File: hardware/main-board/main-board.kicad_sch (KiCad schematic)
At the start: 58 parts, among them J14 Top Left(M), J16 Top Right (M), J18 Bottom Left(M), J20 Bottom Right(M), J9 PWR, Q1 MMBFJ201, U1 TL074, U2 AS3340, U3 79L05, U4 LP2950

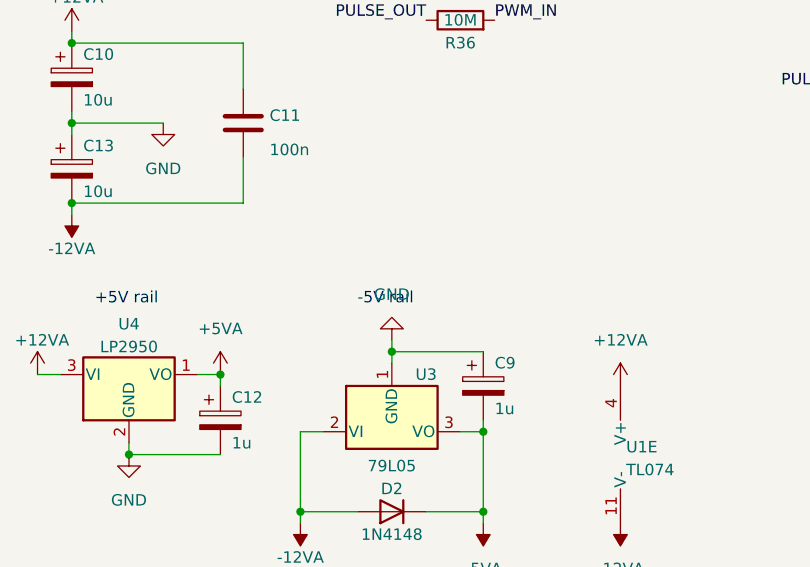
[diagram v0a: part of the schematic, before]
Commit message: chore: git improvements
Using git submodules for managing shared libraries.
Extracted a shared release workflow build to centralise this common
aspect.
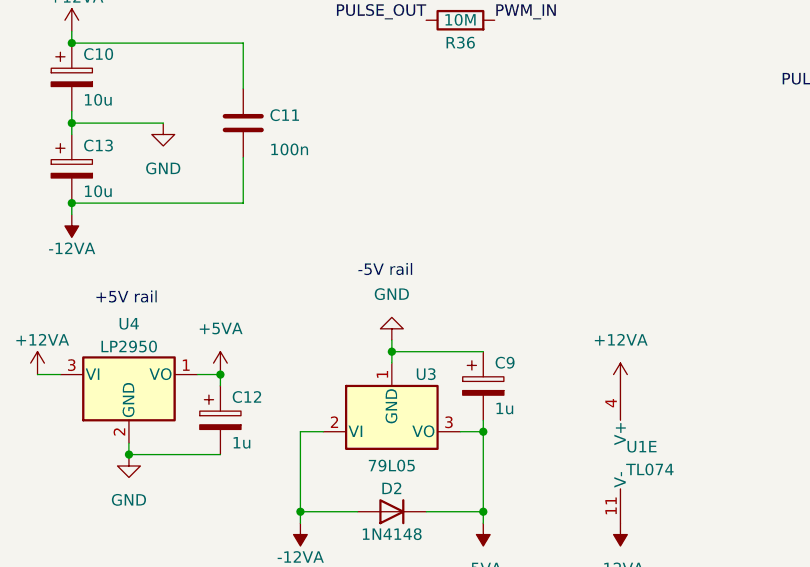
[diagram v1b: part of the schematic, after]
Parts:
- J9: footprint Eurorack Common:SHDR10W50P254_2X5_2020X850X920P -> Eurorack Common:Eurorack Power Header (10 pin); symbol Connector_Generic:Conn_02x05_Odd_Even -> Eurorack Common:Eurorack_Power_Header_(10_pin)
- Q1: symbol cem-3340:MMBFJ201 -> Eurorack Common:MMBFJ201
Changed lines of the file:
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@@
 	(text "-5V rail"
 		(exclude_from_sim no)
-		(at 130.81 163.83 0)
+		(at 130.81 160.782 0)
 		(effects
 			(font
@@
 	)
 	(symbol
-		(lib_id "Connector_Generic:Conn_02x05_Odd_Even")
+		(lib_id "Eurorack Common:Eurorack_Power_Header_(10_pin)")
 		(at 115.57 104.14 0)
 		(unit 1)
@@
 			)
 		)
-		(property "Footprint" "Eurorack Common:SHDR10W50P254_2X5_2020X850X920P"
+		(property "Footprint" "Eurorack Common:Eurorack Power Header (10 pin)"
 			(at 115.57 104.14 0)
 			(effects
@@
 	)
 	(symbol
-		(lib_id "cem-3340:MMBFJ201")
+		(lib_id "Eurorack Common:MMBFJ201")
 		(at 212.09 40.64 0)
 		(unit 1)

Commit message: feature: docs
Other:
- title: (none) -> CEM3340 VCO - Main Board
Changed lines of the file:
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@@
 	(generator_version "9.0")
 	(paper "A4")
+	(title_block
+		(title "CEM3340 VCO - Main Board")
+		(date "2025-11-05")
+		(rev "v1.0.0")
+	)
 	(text "Power decoupling"
 		(exclude_from_sim no)

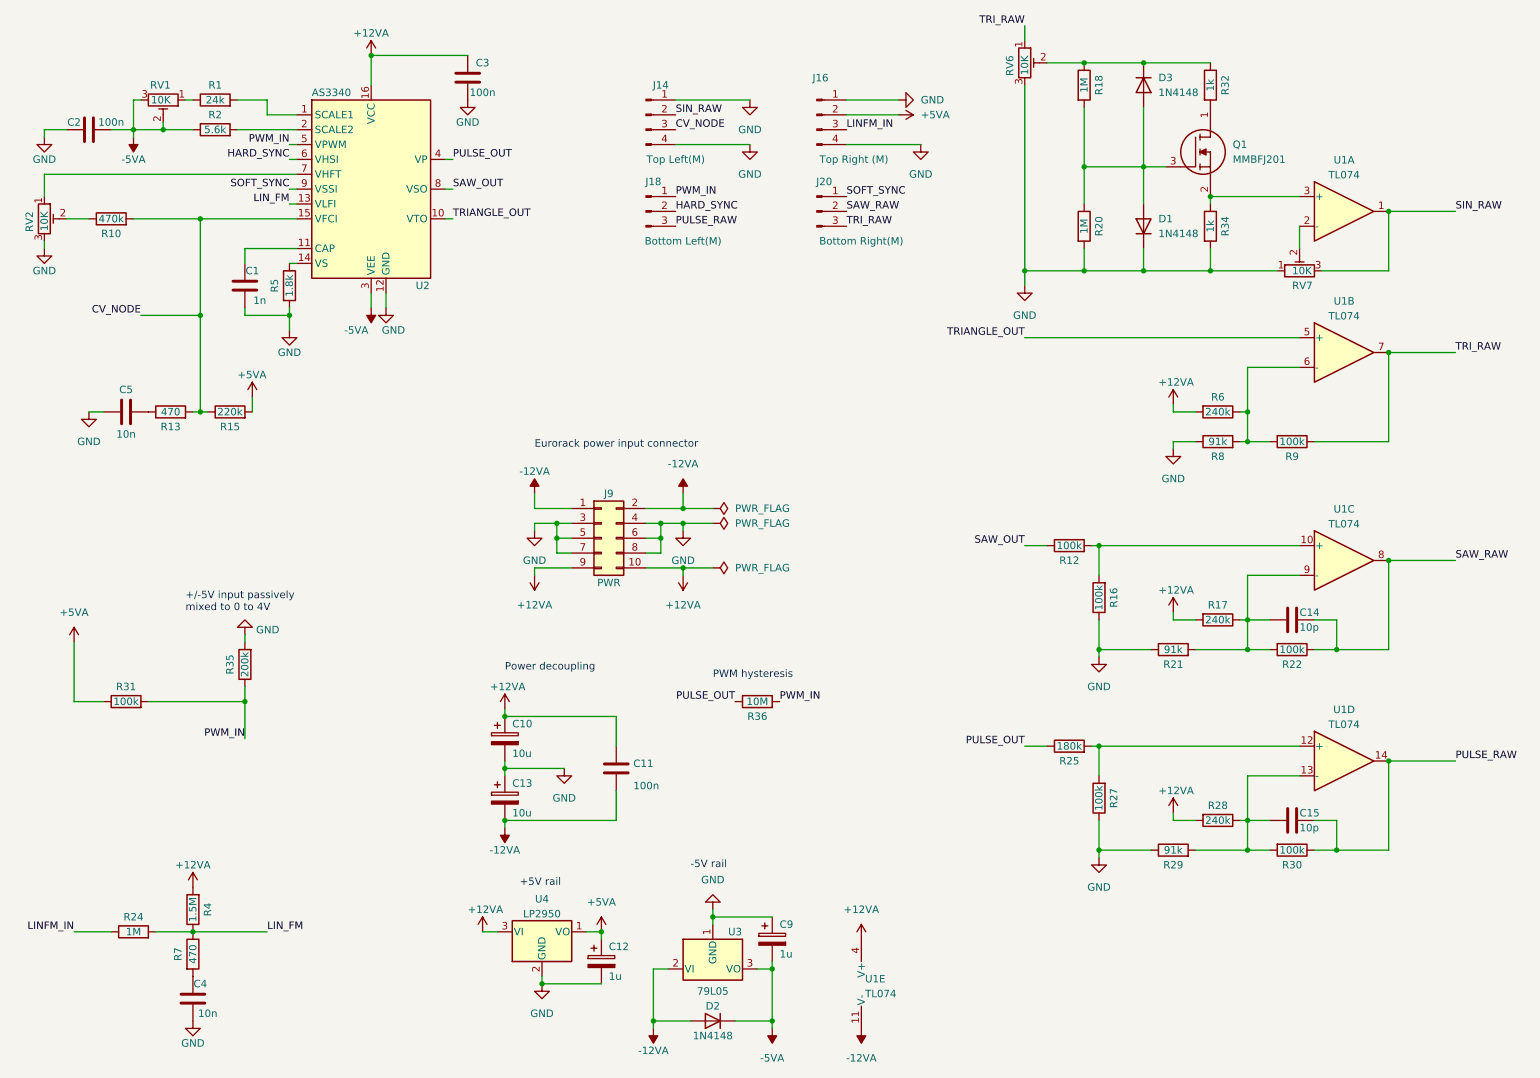
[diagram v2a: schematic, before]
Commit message: feature: improve docs + front panel design
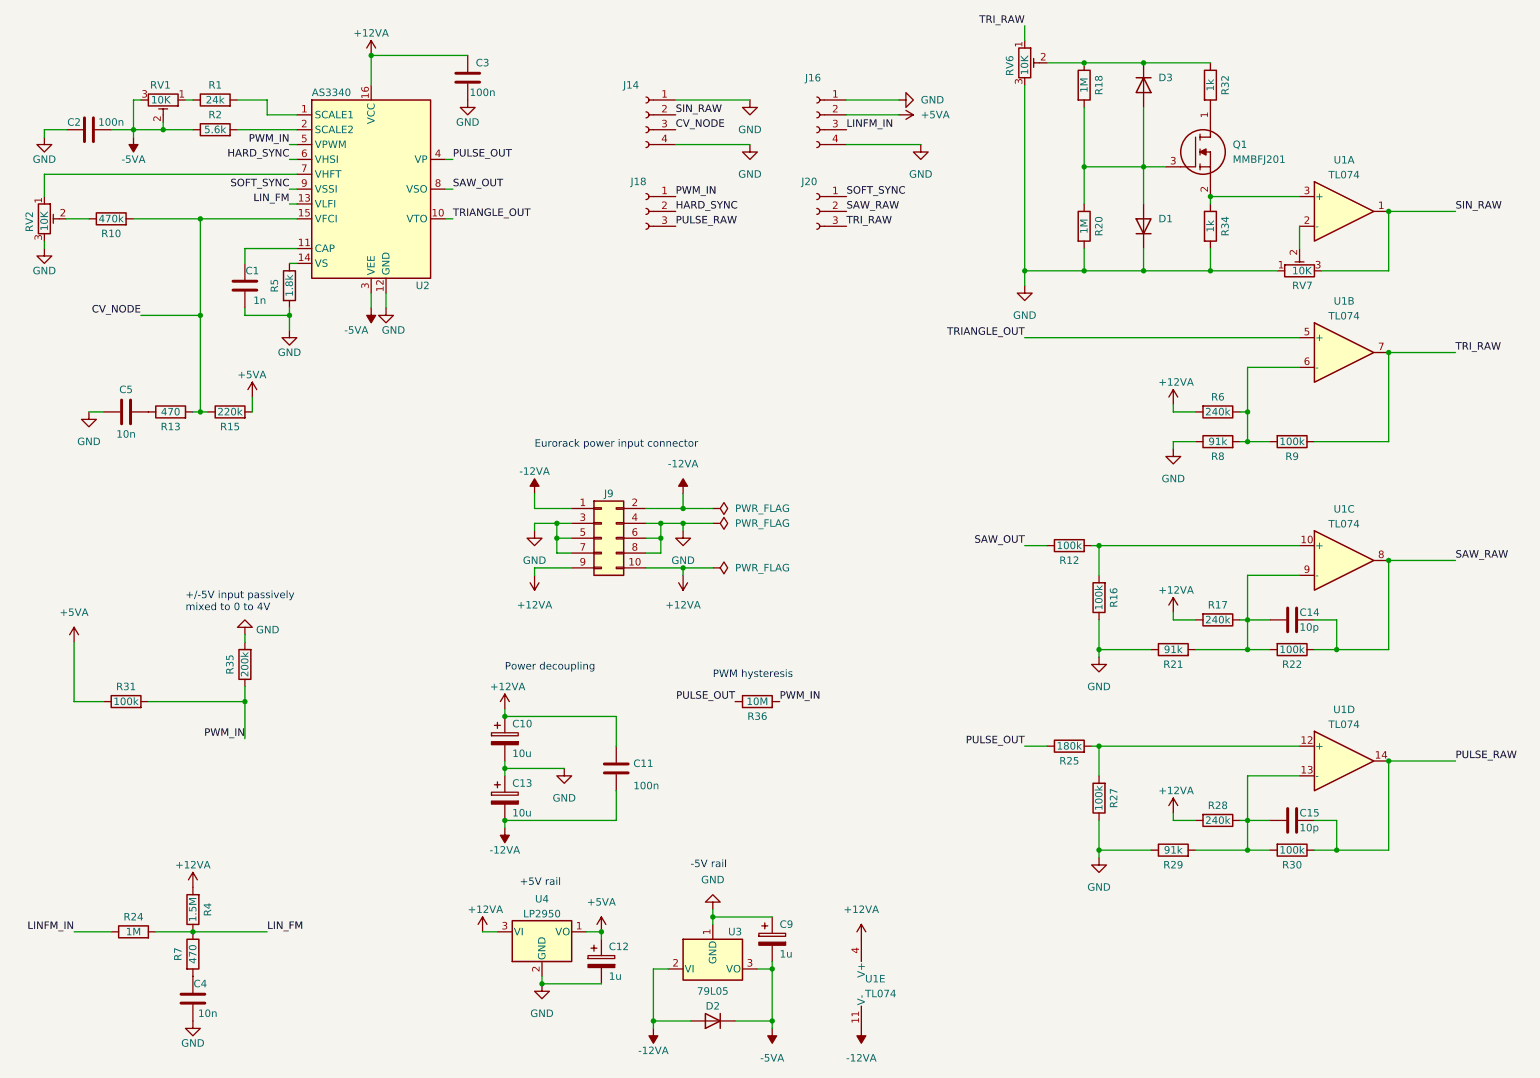
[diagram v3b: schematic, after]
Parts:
- C1: footprint Capacitor_THT:C_Rect_L4.6mm_W2.0mm_P2.50mm_MKS02_FKP02 -> Eurorack Common:C_Disc_D3.4mm_W2.1mm_P2.50mm; Note (none) -> C0G/NP0 ceramic, 2.5mm pitch; Reference_Part (none) -> C320C102J1G5TA; Tolerance (none) -> 5%
- C10, C13: footprint Capacitor_THT:CP_Radial_D5.0mm_P2.00mm -> Eurorack Common:CP_Radial_D5.0mm_H11.0mm_P2.00mm; Note (none) -> Electrolytic, min. 25V, *max height 11mm*, diameter 5mm, pi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; Reference_Part (none) -> ESH106M050AC3AA; Tolerance (none) -> 20%
- C11, C2, C3: footprint Capacitor_THT:C_Rect_L4.6mm_W3.0mm_P2.50mm_MKS02_FKP02 -> Eurorack Common:C_Disc_D3.4mm_W2.1mm_P2.50mm; Note (none) -> X7R ceramic, 2.5mm pitch; Reference_Part (none) -> C320C104K5R5TA; Tolerance (none) -> 5%
- C12, C9: footprint Capacitor_THT:CP_Radial_D4.0mm_P1.50mm -> Eurorack Common:CP_Radial_D4.0mm_P1.50mm; Note (none) -> Electrolytic, min. 25V, *max height 11mm*, diameter 4mm, pi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; Reference_Part (none) -> UST1H010MDD; Tolerance (none) -> 20%
- C14, C15: footprint Capacitor_THT:C_Rect_L4.0mm_W2.5mm_P2.50mm -> Eurorack Common:C_Disc_D3.4mm_W2.1mm_P2.50mm; Note (none) -> C0G/NP0 ceramic, 2.5mm pitch; Reference_Part (none) -> K100J15C0GF5TL2; Tolerance (none) -> 5%
- C4, C5: footprint Capacitor_THT:C_Rect_L4.6mm_W3.0mm_P2.50mm_MKS02_FKP02 -> Eurorack Common:C_Disc_D3.4mm_W2.1mm_P2.50mm; Note (none) -> X7R ceramic, 2.5mm pitch; Reference_Part (none) -> C322C103K1R5TA; Tolerance (none) -> 5%
- D1, D2, D3: value 1N4148 -> ~; footprint Diode_THT:D_DO-35_SOD27_P7.62mm_Horizontal -> Eurorack Common:D_DO-35_SOD27_P7.62mm_Horizontal; Reference_Part (none) -> 1N4148
- J14: value Top Left(M) -> ~; footprint Connector_PinHeader_2.54mm:PinHeader_1x04_P2.54mm_Vertical -> Eurorack Common:PinSocket_1x04_P2.54mm_Vertical; symbol Connector:Conn_01x04_Pin -> Connector:Conn_01x04_Socket; Reference_Part (none) -> 1x4 socket header
- J16: value Top Right (M) -> ~; footprint Connector_PinHeader_2.54mm:PinHeader_1x04_P2.54mm_Vertical -> Eurorack Common:PinSocket_1x04_P2.54mm_Vertical; symbol Connector:Conn_01x04_Pin -> Connector:Conn_01x04_Socket; Reference_Part (none) -> 1x4 socket header
- J18: value Bottom Left(M) -> ~; footprint Connector_PinHeader_2.54mm:PinHeader_1x03_P2.54mm_Vertical -> Eurorack Common:PinSocket_1x03_P2.54mm_Vertical; symbol Connector:Conn_01x03_Pin -> Connector:Conn_01x03_Socket; Reference_Part (none) -> 1x3 socket header
- J20: value Bottom Right(M) -> ~; footprint Connector_PinHeader_2.54mm:PinHeader_1x03_P2.54mm_Vertical -> Eurorack Common:PinSocket_1x03_P2.54mm_Vertical; symbol Connector:Conn_01x03_Pin -> Connector:Conn_01x03_Socket; Reference_Part (none) -> 1x3 socket header
- J9: value PWR -> ~; Note (none) -> The keyed shrouded headers reduce the chance of powering in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; Reference_Part (none) -> PRT-08506
- Q1: footprint Package_TO_SOT_SMD:SOT-23_Handsoldering -> Eurorack Common:SOT-23_Handsoldering; Reference_Part (none) -> MMBFJ201
- R1, R32, R34: footprint Resistor_THT:R_Axial_DIN0207_L6.3mm_D2.5mm_P7.62mm_Horizontal -> Eurorack Common:R_Axial_DIN0207_L6.3mm_D2.5mm_P7.62mm_Horizontal; Reference_Part (none) -> MF1/4DC1001F; Tolerance (none) -> 1%
- R10: footprint Resistor_THT:R_Axial_DIN0207_L6.3mm_D2.5mm_P7.62mm_Horizontal -> Eurorack Common:R_Axial_DIN0207_L6.3mm_D2.5mm_P7.62mm_Horizontal; Reference_Part (none) -> RK73H2ATTD4703F; Tolerance (none) -> 1%
- R12, R16, R22, R27, R30, R31, R9: footprint Resistor_THT:R_Axial_DIN0207_L6.3mm_D2.5mm_P7.62mm_Horizontal -> Eurorack Common:R_Axial_DIN0207_L6.3mm_D2.5mm_P7.62mm_Horizontal; Reference_Part (none) -> MF1/4DC1003F; Tolerance (none) -> 1%
- R13, R7: footprint Resistor_THT:R_Axial_DIN0207_L6.3mm_D2.5mm_P7.62mm_Horizontal -> Eurorack Common:R_Axial_DIN0207_L6.3mm_D2.5mm_P7.62mm_Horizontal; Reference_Part (none) -> MF1/4DC4700F; Tolerance (none) -> 1%
- R15: footprint Resistor_THT:R_Axial_DIN0207_L6.3mm_D2.5mm_P7.62mm_Horizontal -> Eurorack Common:R_Axial_DIN0207_L6.3mm_D2.5mm_P7.62mm_Horizontal; Reference_Part (none) -> MF1/4DC2203F; Tolerance (none) -> 1%
- R17, R28, R6: footprint Resistor_THT:R_Axial_DIN0207_L6.3mm_D2.5mm_P7.62mm_Horizontal -> Eurorack Common:R_Axial_DIN0207_L6.3mm_D2.5mm_P7.62mm_Horizontal; Reference_Part (none) -> MF1/4DC2403F; Tolerance (none) -> 1%
- R18, R20, R24: footprint Resistor_THT:R_Axial_DIN0207_L6.3mm_D2.5mm_P7.62mm_Horizontal -> Eurorack Common:R_Axial_DIN0207_L6.3mm_D2.5mm_P7.62mm_Horizontal; Reference_Part (none) -> MF1/4DC1004F; Tolerance (none) -> 1%
- R2, R5: footprint Resistor_THT:R_Axial_DIN0207_L6.3mm_D2.5mm_P7.62mm_Horizontal -> Eurorack Common:R_Axial_DIN0207_L6.3mm_D2.5mm_P7.62mm_Horizontal; Reference_Part (none) -> MF1/4DC1801F; Tolerance (none) -> 1%
- R21, R29, R8: footprint Resistor_THT:R_Axial_DIN0207_L6.3mm_D2.5mm_P7.62mm_Horizontal -> Eurorack Common:R_Axial_DIN0207_L6.3mm_D2.5mm_P7.62mm_Horizontal; Reference_Part (none) -> MF1/4DC9102F; Tolerance (none) -> 1%
- R25: footprint Resistor_THT:R_Axial_DIN0207_L6.3mm_D2.5mm_P7.62mm_Horizontal -> Eurorack Common:R_Axial_DIN0207_L6.3mm_D2.5mm_P7.62mm_Horizontal; Reference_Part (none) -> MF1/4DC1803F; Tolerance (none) -> 1%
- R35: footprint Resistor_THT:R_Axial_DIN0207_L6.3mm_D2.5mm_P7.62mm_Horizontal -> Eurorack Common:R_Axial_DIN0207_L6.3mm_D2.5mm_P7.62mm_Horizontal; Reference_Part (none) -> MF1/4DC2003F; Tolerance (none) -> 1%
- R36: footprint Resistor_THT:R_Axial_DIN0207_L6.3mm_D2.5mm_P7.62mm_Horizontal -> Eurorack Common:R_Axial_DIN0207_L6.3mm_D2.5mm_P7.62mm_Horizontal; Reference_Part (none) -> HHV-25FR-52-10M; Tolerance (none) -> 1%
- R4: footprint Resistor_THT:R_Axial_DIN0207_L6.3mm_D2.5mm_P7.62mm_Horizontal -> Eurorack Common:R_Axial_DIN0207_L6.3mm_D2.5mm_P7.62mm_Horizontal; Reference_Part (none) -> MF1/4DC1504F; Tolerance (none) -> 1%
- RV1, RV2, RV6, RV7: footprint Potentiometer_THT:Potentiometer_Bourns_3296W_Vertical -> Eurorack Common:Potentiometer_Bourns_3296W_Vertical; symbol Device:R_Potentiometer_Trim -> Eurorack Common:R_Potentionmeter_Trim_Bournes; Note (none) -> These are top adjusted. You could use the 3296X, which is s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; Reference_Part (none) -> 3296W
- U1: footprint Package_DIP:DIP-14_W7.62mm_LongPads -> Eurorack Common:DIP-14_W7.62mm; Reference_Part (none) -> Generic PDIP
- U2: footprint Package_DIP:DIP-16_W7.62mm_LongPads -> Eurorack Common:DIP-16_W7.62mm; Reference_Part (none) -> AS3340
- U3: footprint Package_TO_SOT_THT:TO-92_Inline -> Eurorack Common:TO-92_Inline; Reference_Part (none) -> L79L05ACZ
- U4: footprint Package_TO_SOT_THT:TO-92_Inline -> Eurorack Common:TO-92_Inline; Reference_Part (none) -> LP2950CZ-5.0/LFT1
